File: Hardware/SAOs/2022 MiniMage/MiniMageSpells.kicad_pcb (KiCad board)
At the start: 2 copper layers, 46.4 x 70.4 mm, 10 parts, among them X1 Badgelife_sao_connector_v169b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

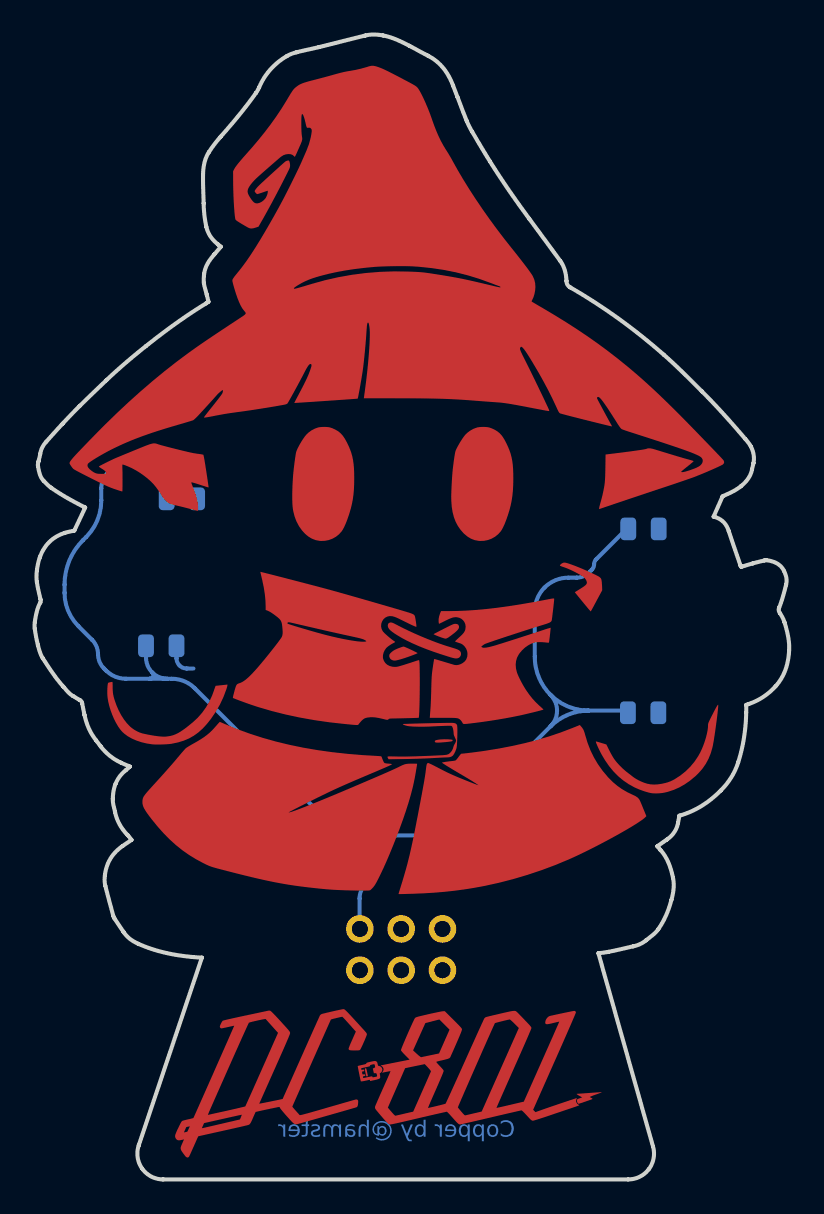
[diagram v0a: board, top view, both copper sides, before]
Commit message: Adding panel for SAOs
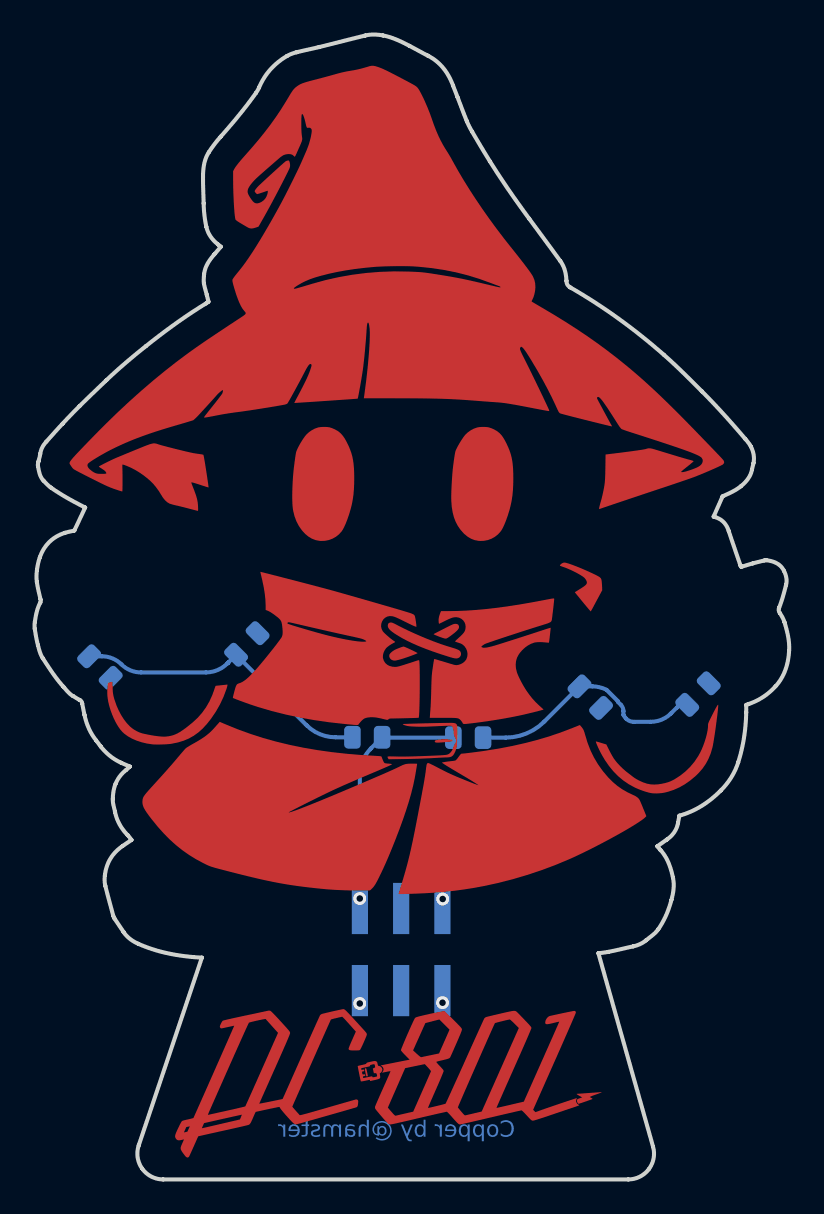
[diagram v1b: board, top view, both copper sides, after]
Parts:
- added REF**: Tab, kikit:Tab, F.Cu at (134.3, 128.7)
- X1: footprint common_fp:Badgelife-Shitty-v1.69bis -> Connector_PinHeader_2.54mm:PinHeader_2x03_P2.54mm_Vertical_SMD; moved to B.Cu
- moved D1 10.9 mm to (146.0, 98.5), turned to 135 degrees
- moved D4 9.78 mm to (124.8, 95.2), turned to -135 degrees
- moved R2 6.06 mm to (132.2, 100.9)
- moved R1 6.06 mm to (138.4, 101.0)
- moved D3 4.00 mm to (115.8, 96.6), turned to 135 degrees
- moved D2 3.56 mm to (152.6, 98.3), turned to -135 degrees
- turned X1 to -90 degrees
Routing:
- net Net-(D3-Pad2): track 41.0 -> 18.6 mm
- net Net-(D1-Pad2): track 32.0 -> 15.2 mm
- net +3V3: track 10.3 -> 17.2 mm, vias 0 -> 1
- net GND: track 2.16 -> 0.00 mm, vias 0 -> 1
- net unconnected-(X1-Pad6): vias 0 -> 1
- net unconnected-(X1-Pad5): vias 0 -> 1
